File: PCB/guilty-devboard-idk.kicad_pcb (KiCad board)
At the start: 6 copper layers, 17.8 x 33.2 mm, 60 parts, among them J1 USB_C_Receptacle_USB2.0_16P, Q1 SP2038CNQ, U1 nRF54LM20A-QGAA, U2 SGM40567-4.2XG/TR, U3 Xiao nRF52840 Connectors, U5 FH9261-G3JH, U6 BD83070GWL-E2, Y1 32MHz, Y2 32.768kHz

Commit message: use way smaller crystals and redo with space for bigger cap/inductor
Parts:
- C1: footprint Capacitor_SMD:C_0201_0603Metric -> Capacitor_SMD:C_0402_1005Metric
- L3: footprint Inductor_SMD:L_0201_0603Metric -> Inductor_SMD:L_0603_1608Metric
- Y1, Y2: footprint Crystal:Crystal_SMD_2016-4Pin_2.0x1.6mm -> Crystal:Crystal_SMD_1210-4Pin_1.2x1.0mm
- moved C19 16.6 mm to (90.2, 47.6), turned to 180 degrees
- moved C1 3.47 mm to (88.7, 55.0), turned to 90 degrees
- moved L3 2.33 mm to (89.5, 63.2), turned to 90 degrees
- moved C23 1.47 mm to (88.5, 62.5)
- moved D6 1.38 mm to (87.5, 62.7)
- moved Y2 0.78 mm to (86.1, 62.8)
- moved R6 0.48 mm to (86.0, 65.5), turned to 180 degrees
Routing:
- net +3V3: track 9.17 -> 20.0 mm, vias 5 -> 7
- net Net-(U6-LX1): track 0.71 -> 4.25 mm
- net Net-(U1A-XC2): track 3.04 -> 0.00 mm
- net Net-(U5-VM): track 3.83 -> 1.65 mm
- net Net-(U1A-P1.20): track 2.80 -> 1.32 mm
- net Net-(U6-REF): track 3.89 -> 2.42 mm
- net Net-(U1A-XC1): track 1.47 -> 0.16 mm, vias 2 -> 1
- net GND: track 31.8 -> 32.8 mm, vias 41 -> 39
- net +BATT: track 40.0 -> 39.3 mm
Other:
- board text added: ":3"

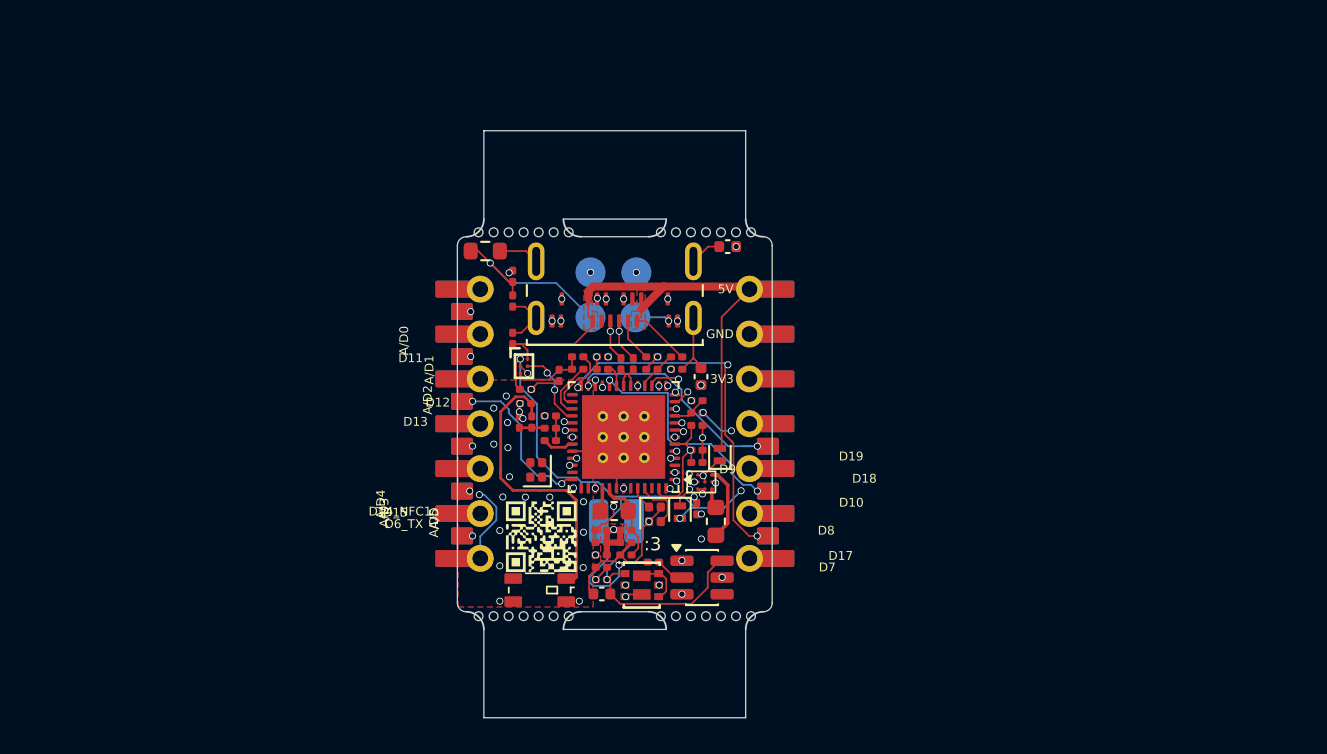
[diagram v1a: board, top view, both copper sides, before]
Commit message: reroute antenna/rf filter
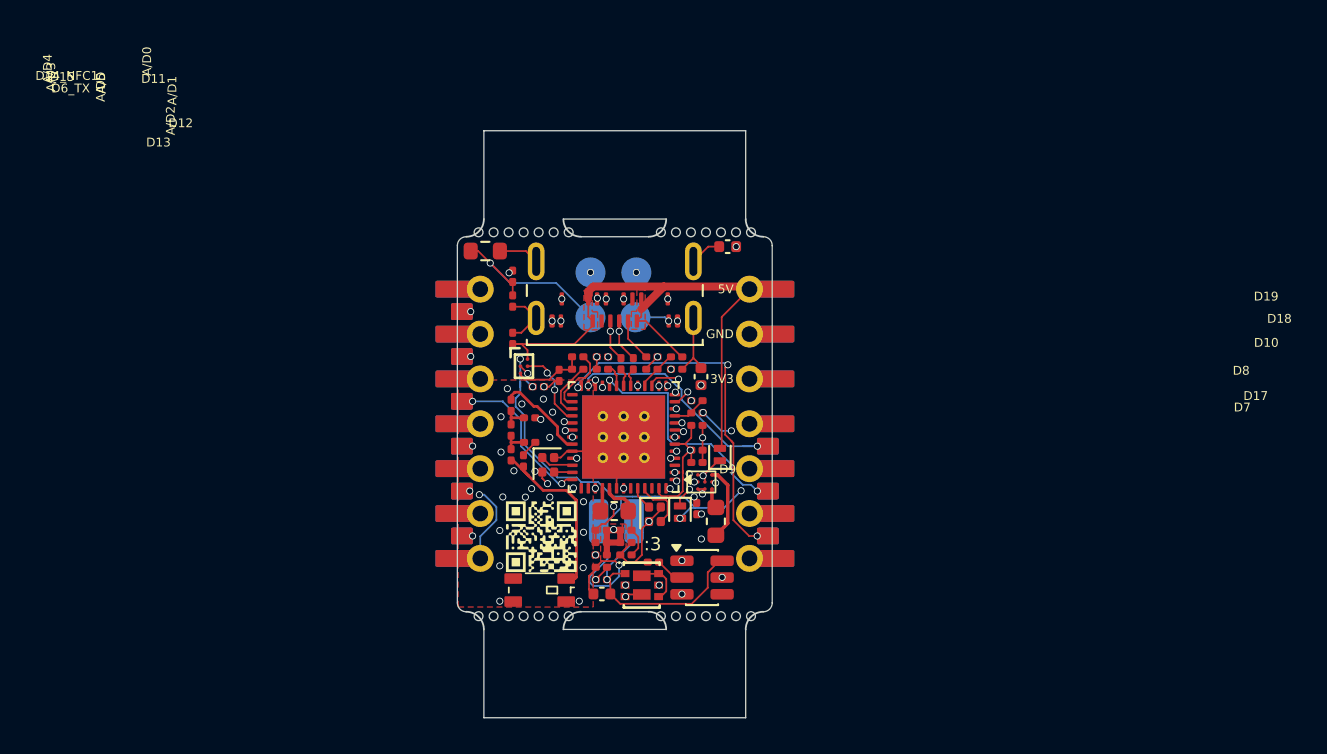
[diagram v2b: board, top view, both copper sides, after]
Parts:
- moved C3 3.25 mm to (78.7, 59.8), turned to -90 degrees
- moved L5 2.98 mm to (78.0, 56.6), turned to -90 degrees
- moved L4 2.22 mm to (78.0, 58.0), turned to -90 degrees
- moved L1 2.19 mm to (78.0, 59.4), turned to -90 degrees
- moved C15 1.29 mm to (79.0, 58.7), turned to 180 degrees
- moved C18 1.18 mm to (79.0, 57.3), turned to 180 degrees
- moved Y1 0.74 mm to (80.0, 60.0), turned to 0 degrees
- moved C17 0.74 mm to (79.5, 55.6)
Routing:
- net Net-(AE1-FEED): track 16.8 -> 10.3 mm
- net /ANT: track 1.80 -> 5.25 mm
- net Net-(U1A-XC1): track 0.16 -> 1.89 mm, vias 1 -> 0
- net /P1.09_D6: track 16.0 -> 14.8 mm
- net Net-(U1A-XC2): track 0.00 -> 1.04 mm
- net GND: track 32.8 -> 33.7 mm, vias 39 -> 41
- net +BATT: track 39.3 -> 39.0 mm, vias 6 -> 7

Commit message: tbh i have no idea what i cchanged but uh sure commit why not
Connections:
- Y1 pad 4: GND -> (no net)
- Y2 pad 4: GND -> (no net)
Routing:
- net GND: track 33.7 -> 31.4 mm

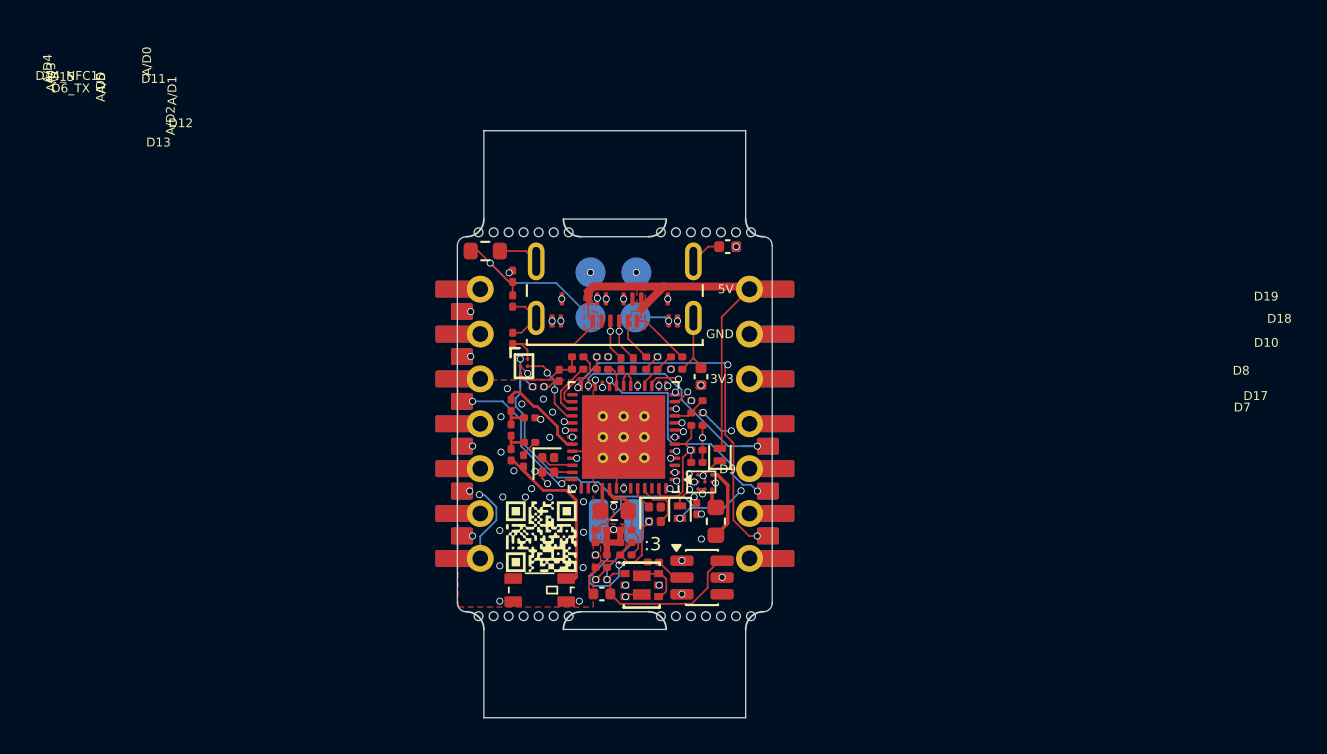
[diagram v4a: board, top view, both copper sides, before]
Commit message: route tca9536 and stuffffff
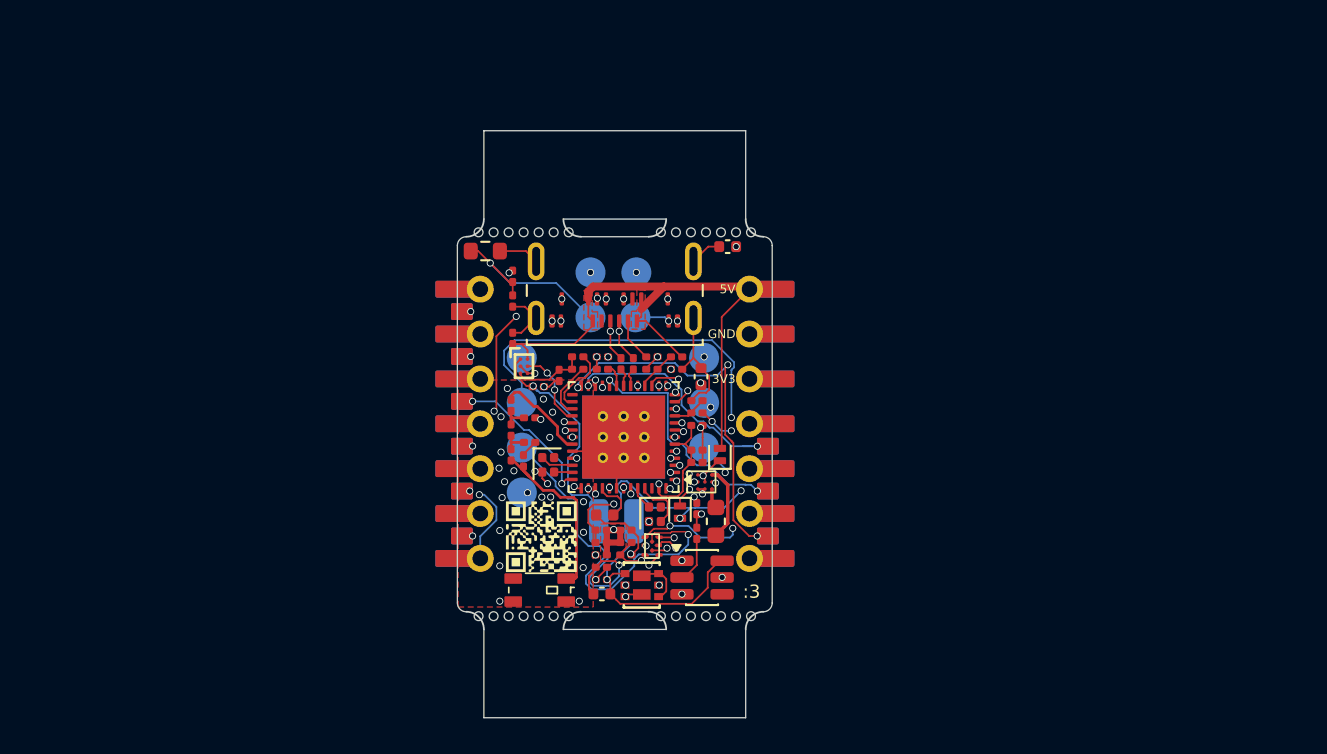
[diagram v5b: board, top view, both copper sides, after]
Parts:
- added U4: TCA9536, guilty-devboard-idk:TCA9536, F.Cu at (85.9, 64.1)
- L6: footprint Inductor_SMD:L_0603_1608Metric -> Inductor_SMD:L_0402_1005Metric
- U3: footprint guilty-devboard-idk:Xiao nRF52840 Plus pads -> guilty-devboard-idk:Guilty Devboard Xrd pads
- moved R6 2.95 mm to (88.5, 63.9), turned to 90 degrees
- moved L6 0.58 mm to (83.2, 62.8), turned to 180 degrees
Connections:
- U1 pad 3: unconnected-(U1D-P2.03-Pad3) -> /IO_EXT_INT
- U1 pad 40: unconnected-(U1C-P1.16-Pad40) -> /P1.16_D24
- U1 pad 41: unconnected-(U1C-P1.18-Pad41) -> /P1.18_D25
- U1 pad 47: unconnected-(U1C-P1.19-Pad47) -> /P1.19_D26
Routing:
- net /IO_EXT_P0_D21: track 0.00 -> 32.9 mm, vias 0 -> 3
- net /P1.16_D24: track 0.00 -> 27.2 mm, vias 0 -> 5
- net /IO_EXT_P1_D22: track 0.00 -> 20.7 mm, vias 0 -> 1
- net /P1.19_D26: track 0.00 -> 13.1 mm, vias 0 -> 2
- net /P1.18_D25: track 0.00 -> 12.3 mm, vias 0 -> 2
- net /P1.31_A/D5_I2C_SCL: track 14.2 -> 26.3 mm, vias 1 -> 4
- net /P1.30_A/D4_I2C_SDA: track 12.9 -> 22.5 mm, vias 1 -> 2
- net /IO_EXT_INT: track 0.00 -> 8.96 mm, vias 0 -> 2
- net /IO_EXT_P2_D23: track 0.00 -> 8.54 mm, vias 0 -> 2
- net Net-(U1A-DECD): track 4.92 -> 8.60 mm, vias 0 -> 2
- net +BATT: track 39.0 -> 42.3 mm, vias 7 -> 6
- net GND: track 31.4 -> 33.0 mm, vias 41 -> 37
- net Net-(U1A-DECRF): track 6.42 -> 7.61 mm
- net Net-(U5-VM): track 1.65 -> 2.82 mm
- net Net-(U1A-DCC): track 1.34 -> 2.51 mm
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
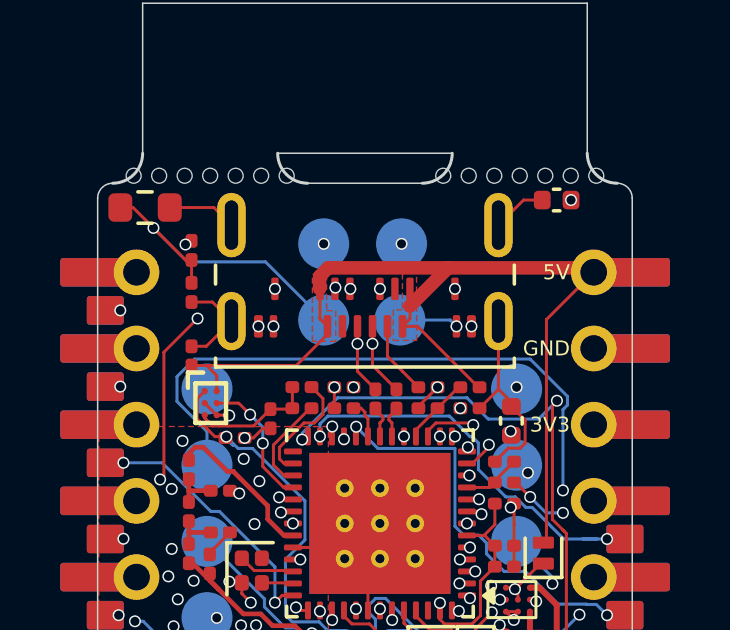
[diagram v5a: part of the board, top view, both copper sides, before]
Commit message: add ferrite bead to shield usb-c
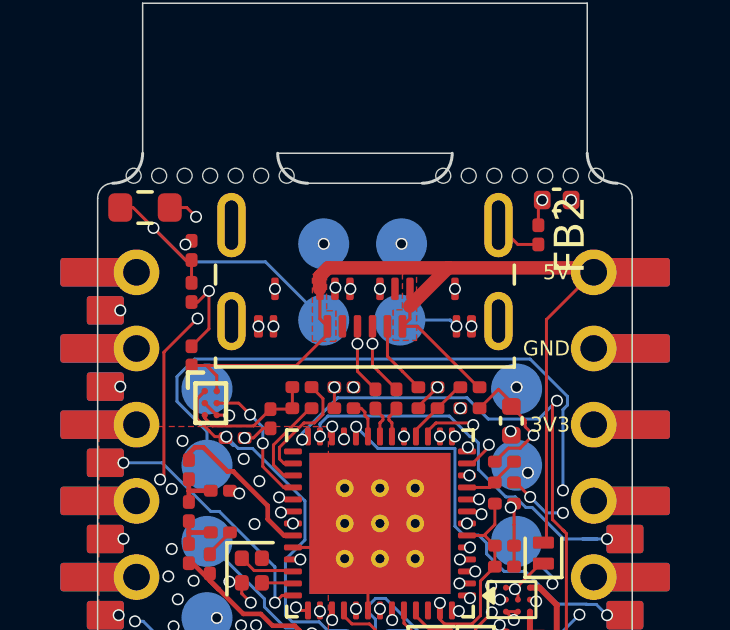
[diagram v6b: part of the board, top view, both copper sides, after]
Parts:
- added FB2: FerriteBead, Inductor_SMD:L_0201_0603Metric, F.Cu at (89.6, 48.8)
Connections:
- J1 pad SH: GND -> Net-(J1-SHIELD)
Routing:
- net Net-(J1-SHIELD): track 0.00 -> 16.9 mm
- net GND: track 33.0 -> 28.3 mm, vias 37 -> 41

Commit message: improve qr code
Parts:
- removed the G*** at (79.7, 64.1)

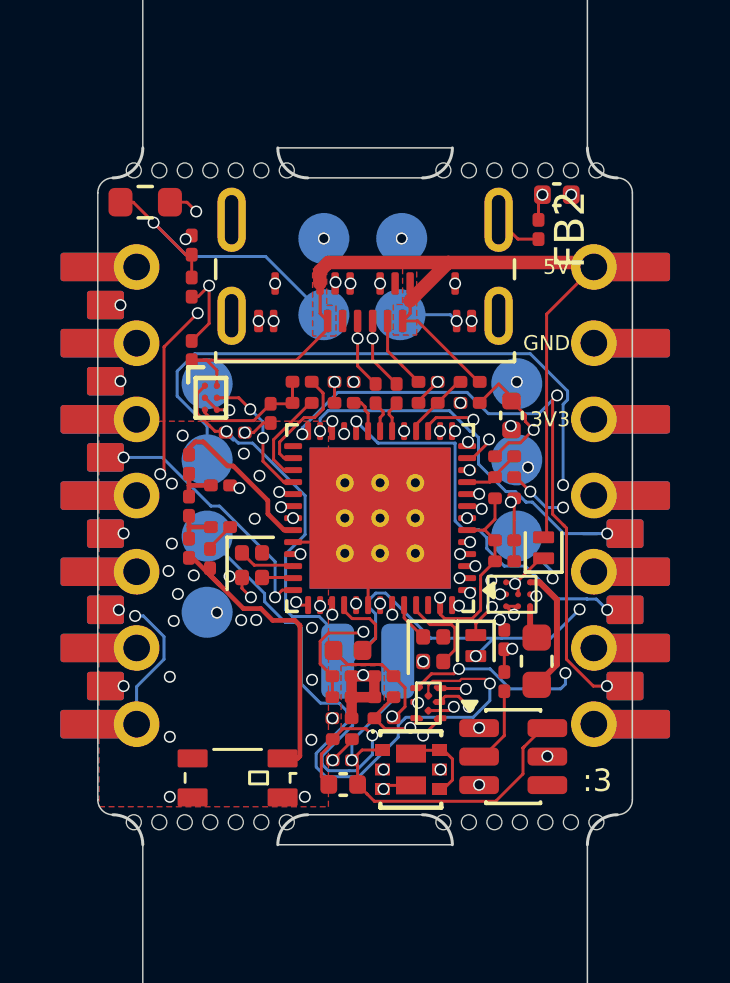
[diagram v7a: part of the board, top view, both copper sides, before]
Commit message: update qr codes with link shortener, fix footprint, update bom with antenna
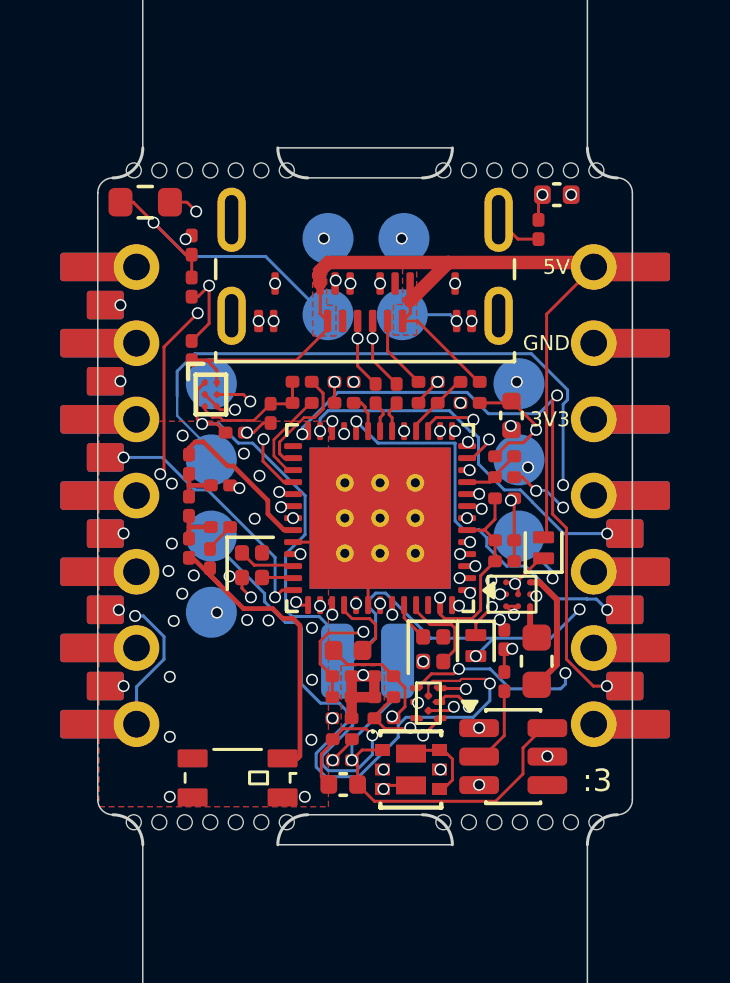
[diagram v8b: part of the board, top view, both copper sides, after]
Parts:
- removed G***: LOGO, LOGO
- moved U2 0.11 mm to (78.7, 54.3)
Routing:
- net +BATT: track 42.3 -> 40.0 mm
- net /P1.05_A/D2: track 10.2 -> 12.0 mm
- net GND: track 28.3 -> 26.9 mm
- net /P1.31_A/D5_I2C_SCL: track 26.3 -> 25.1 mm
- net /P1.18_D25: track 12.3 -> 11.6 mm
- net /P2.00_SPIM.DCX_UARTE00.RXD: track 6.46 -> 5.76 mm
- net +3V3: track 20.6 -> 19.9 mm
- net -BATT: track 14.1 -> 13.5 mm
- net /FAST_CHARGE_1: track 3.87 -> 4.47 mm
- net /P1.06_A/D3: track 16.0 -> 15.4 mm
- net VBUS: track 34.0 -> 33.5 mm
